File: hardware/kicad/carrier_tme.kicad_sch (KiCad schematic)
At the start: 65 parts, among them J2 Heltec_J2, J3 Heltec_J3, U2 TCA9534PWR

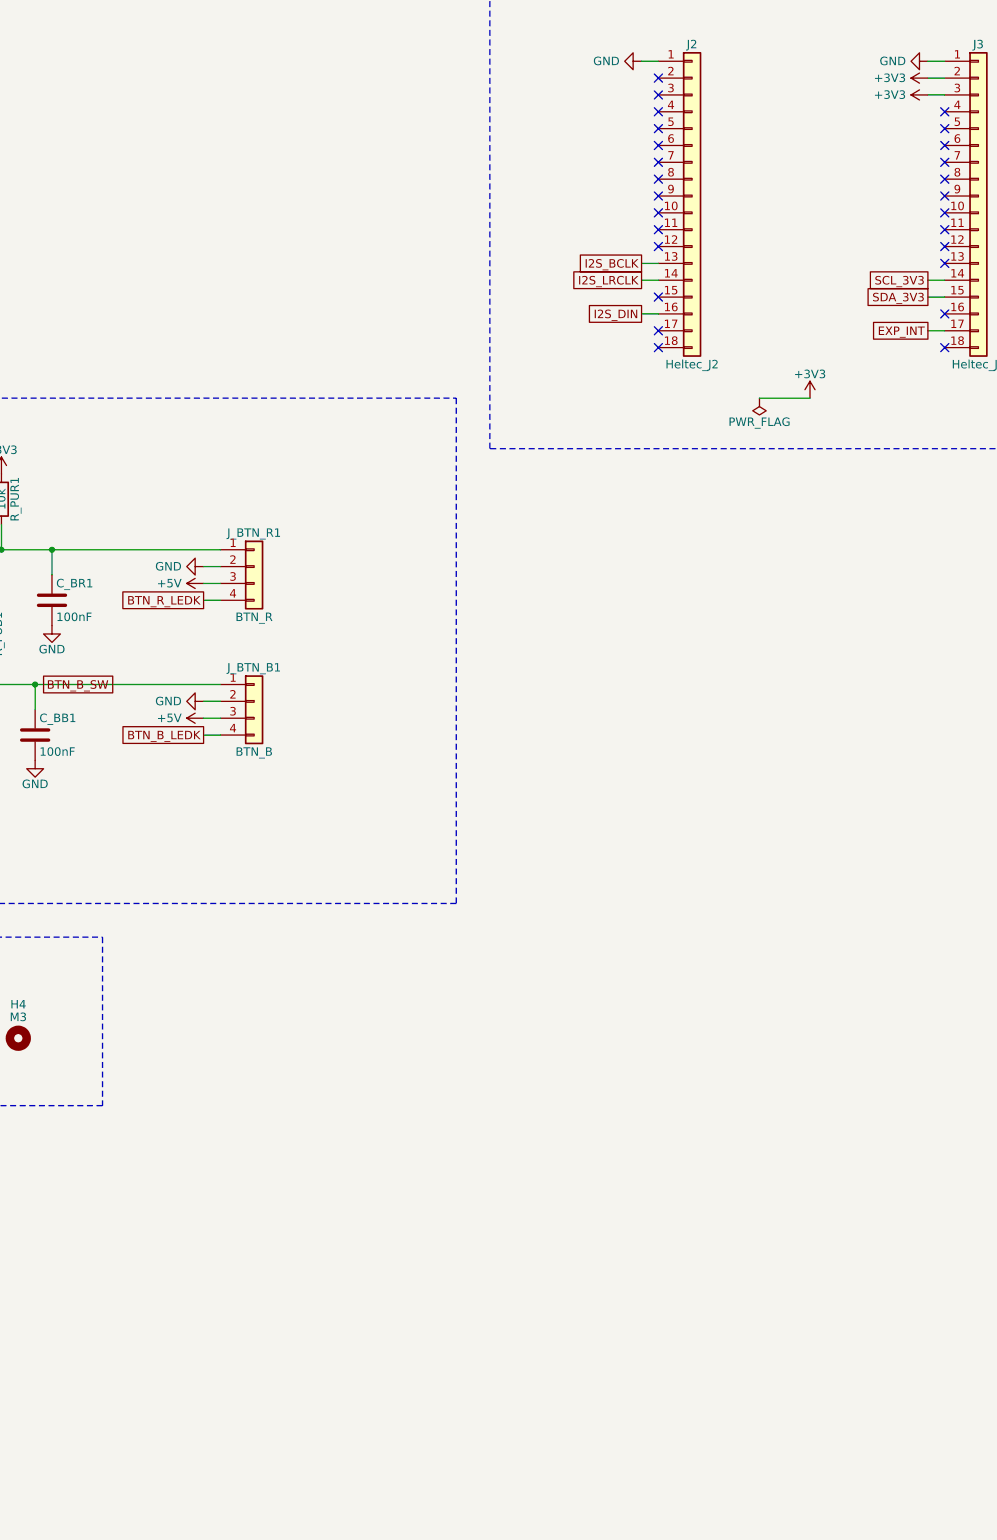
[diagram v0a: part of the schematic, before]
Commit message: hardware: UART debug header on all boards, I2C header and rail test pads on carrier, SDA/SCL pads on pack
Header is 1x3 2.54 mm (GND, MCU TX, MCU RX), hand-soldered, kept out of the BOM.
Carrier uses Heltec UART0 (GPIO43/44), STM32 boards USART1 (PA9/PA10).

Co-Authored-By: Claude Sonnet 5.5 <noreply@anthropic.com>
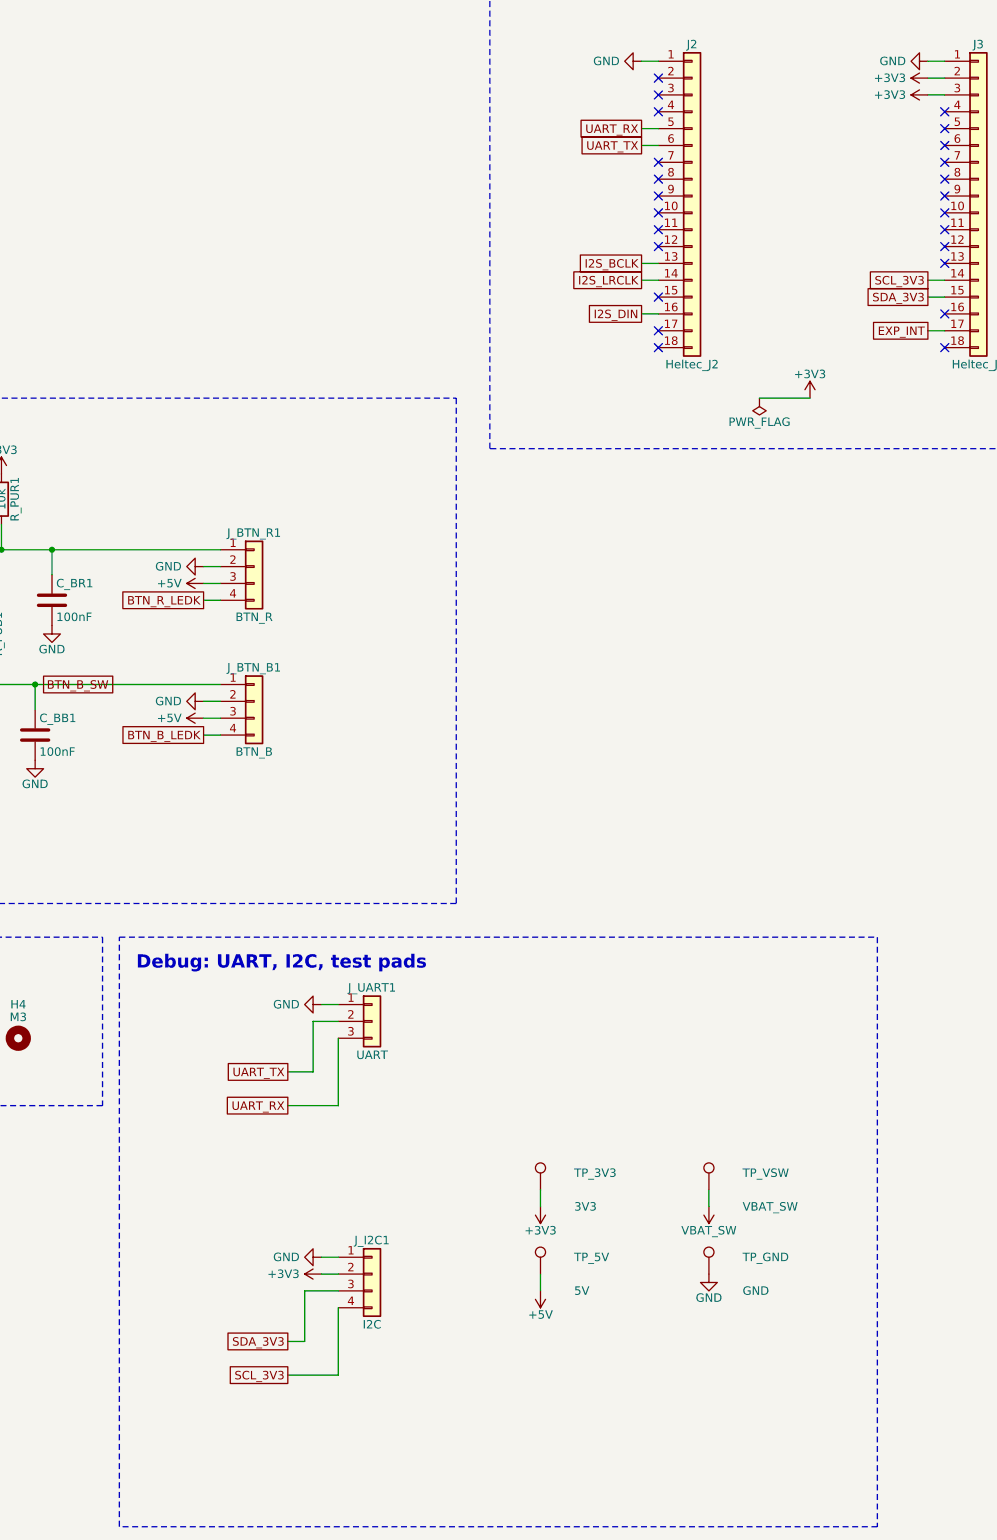
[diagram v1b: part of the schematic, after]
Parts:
- added J_I2C1: I2C, Connector_PinHeader_2.54mm:PinHeader_1x04_P2.54mm_Vertical, symbol Connector_Generic:Conn_01x04
- added J_UART1: UART, Connector_PinHeader_2.54mm:PinHeader_1x03_P2.54mm_Vertical, symbol Connector_Generic:Conn_01x03
- added TP_3V3: 3V3, TestPoint:TestPoint_Pad_D1.5mm, symbol Connector:TestPoint
- added TP_5V: 5V, TestPoint:TestPoint_Pad_D1.5mm, symbol Connector:TestPoint
- added TP_GND: GND, TestPoint:TestPoint_Pad_D1.5mm, symbol Connector:TestPoint
- added TP_VSW: VBAT_SW, TestPoint:TestPoint_Pad_D1.5mm, symbol Connector:TestPoint
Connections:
- net +3V3: now also J_I2C1.2 (Pin_2), TP_3V3.1
- net +5V: now also TP_5V.1
- net GND: now also J_I2C1.1 (Pin_1), J_UART1.1 (Pin_1), TP_GND.1
- net SCL_3V3: now also J_I2C1.4 (Pin_4)
- net SDA_3V3: now also J_I2C1.3 (Pin_3)
- net VBAT_SW: now also TP_VSW.1
- net UART_RX: now reaches J2.5 (Pin_5)
- net UART_RX: now also J_UART1.3 (Pin_3)
- net UART_TX: now reaches J2.6 (Pin_6)
- net UART_TX: now also J_UART1.2 (Pin_2)
- no-connect marks 29 -> 27
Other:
- note added: "Debug: UART, I2C, test pads"

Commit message: hardware: KiCad 10 pipeline fixes, +5V reservoir caps, NS4168 1uF, pack UART header off the holders
KiCad 9 -> 10.0.7 broke the generators even on HEAD:
- gen_sch: libraries moved (hide yes) from effects to the property; read both,
  write it back into effects (KiCad 9 format), so hidden fields stop showing
  on every sheet and stop blocking the schematic router. Add the title block.
- gen_pcb: SetDoNotAllowCopperPour -> SetDoNotAllowZoneFills; copy the symbol's
  Datasheet/Description/Sim fields onto footprints (schematic parity now fails
  DRC); refuse THT pads under bottom-side parts (PTH_UNDER_OK allowlist).
- route.py: Power class routed at +40 um (Freerouting's octagons undercut 0.8 mm
  round ends, KiCad 10 exports no clearance margin), falling back to no margin
  if that leaves a connection unrouted; strip dangling stubs after SES import.
- pack: USB-C shield pin S1 -> SH; pack_tme: VSSOP-10 -> MSOP-10 footprint.

Design changes from the Konnect MCP review and datasheet check:
- carrier: C_5V1 10 uF + C_5V2 100 nF on +5V at J_PWR1 (no local cap before);
  C_AMP2 100 nF -> 1 uF per NS4168 datasheet (100 uF || 1 uF). carrier_tme
  places the new caps clear of its DAC.
- pack/pack_tme: J_UART1 sat under BT4 (bottom-side 18650 holder), caught by
  KiCad 10's pth_inside_courtyard; moved to the right strip, label in pin order.
  The NTC beads stay in the holder window (check ignored, gen_pcb enforces it).
- Docs: ORDERING counts, NS4168/TCA9534/BSS138/1N4148W datasheet check,
  TCA9534 P6/P7 firmware note.

All six boards: ERC 0, DRC 0 (0 unconnected, 0 parity), gerbers ok.

Co-Authored-By: Claude Opus 5.5 <noreply@anthropic.com>
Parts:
- added C_5V1: 10uF, Capacitor_SMD:C_0805_2012Metric_Pad1.18x1.45mm_HandSolder, symbol Device:C
- added C_5V2: 100nF, Capacitor_SMD:C_0805_2012Metric_Pad1.18x1.45mm_HandSolder, symbol Device:C
- C_AMP2: value 100nF -> 1uF
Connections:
- net +5V: now also C_5V1.1, C_5V2.1
- net GND: now also C_5V1.2, C_5V2.2
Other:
- title: (none) -> AirsoftCounter v2 carrier (hand-build)
